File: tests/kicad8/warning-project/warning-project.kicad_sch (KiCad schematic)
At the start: 0 parts

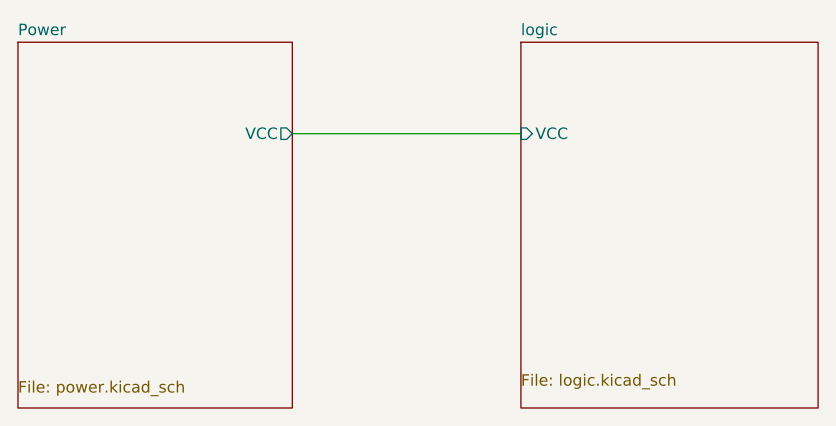
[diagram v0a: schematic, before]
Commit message: [PCBNew][DRC] Implemented CLI version
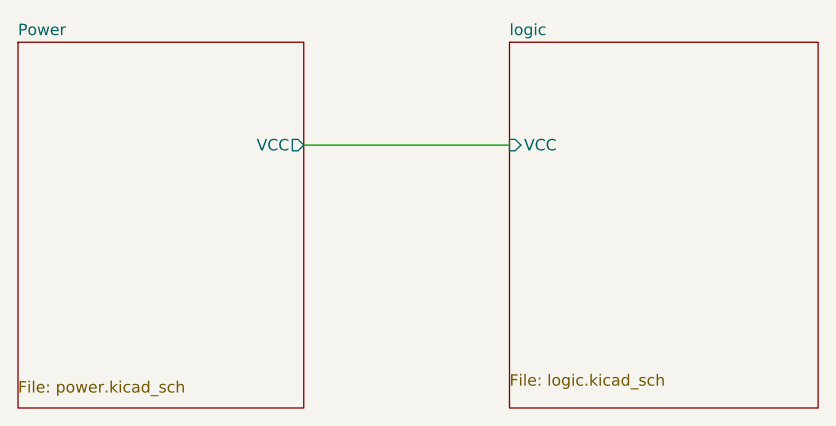
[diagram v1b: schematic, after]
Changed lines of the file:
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@@
-(kicad_sch (version 20230409) (generator eeschema)
-  (paper "A4")
-  (wire (pts (xy 111.76 63.5) (xy 137.16 63.5))
-    (stroke (width 0) (type default))
-  )
-  (sheet (at 81.28 53.34) (size 30.48 40.64)
-    (stroke (width 0) (type solid))
-    (fill (color 0 0 0 0.0000))
-    (property "Sheetname" "Power" (at 81.28 52.7045 0)
-      (effects (font (size 1.27 1.27)) (justify left bottom))
-    )
-    (property "Sheetfile" "power.kicad_sch" (at 81.28 90.9325 0)
-      (effects (font (size 1.27 1.27)) (justify left top))
-    )
-    (pin "VCC" output (at 111.76 63.5 0)
-      (effects (font (size 1.27 1.27)) (justify right))
-    )
-    (instances
-      (project "warning-project"
-        (path "/87c78429-be2b-40ed-8d3b-56cb9666a56f" (page "2"))
-      )
-    )
-  )
-  (sheet (at 137.16 53.34) (size 33.02 40.64)
-    (stroke (width 0) (type solid))
-    (fill (color 0 0 0 0.0000))
-    (property "Sheetname" "logic" (at 137.16 52.7045 0)
-      (effects (font (size 1.27 1.27)) (justify left bottom))
-    )
-    (property "Sheetfile" "logic.kicad_sch" (at 137.16 90.1705 0)
-      (effects (font (size 1.27 1.27)) (justify left top))
-    )
-    (pin "VCC" input (at 137.16 63.5 180)
-      (effects (font (size 1.27 1.27)) (justify left))
-    )
-    (instances
-      (project "warning-project"
-        (path "/87c78429-be2b-40ed-8d3b-56cb9666a56f" (page "3"))
-      )
-    )
-  )
-  (sheet_instances
-    (path "/" (page "1"))
-  )
+(kicad_sch
+	(version 20231120)
+	(generator "eeschema")
+	(generator_version "8.0")
+	(paper "A4")
+	(wire
+		(pts
+			(xy 113.03 64.77) (xy 135.89 64.77)
+		)
+		(stroke
+			(width 0)
+			(type default)
+		)
+	)
+	(sheet
+		(at 81.28 53.34)
+		(size 31.75 40.64)
+		(stroke
+			(width 0)
+			(type solid)
+		)
+		(fill
+			(color 0 0 0 0.0000)
+		)
+		(property "Sheetname" "Power"
+			(at 81.28 52.7045 0)
+			(effects
+				(font
+					(size 1.27 1.27)
+				)
+				(justify left bottom)
+			)
+		)
+		(property "Sheetfile" "power.kicad_sch"
+			(at 81.28 90.9325 0)
+			(effects
+				(font
+					(size 1.27 1.27)
+				)
+				(justify left top)
+			)
+		)
+		(pin "VCC" output
+			(at 113.03 64.77 0)
+			(effects
+				(font
+					(size 1.27 1.27)
+				)
+				(justify right)
+			)
+		)
+		(instances
+			(project "fail-project"
+				(path "/87c78429-be2b-40ed-8d3b-56cb9666a56f"
+					(page "2")
+				)
+			)
+		)
+	)
+	(sheet
+		(at 135.89 53.34)
+		(size 34.29 40.64)
+		(stroke
+			(width 0)
+			(type solid)
+		)
+		(fill
+			(color 0 0 0 0.0000)
+		)
+		(property "Sheetname" "logic"
+			(at 135.89 52.7045 0)
+			(effects
+				(font
+					(size 1.27 1.27)
+				)
+				(justify left bottom)
+			)
+		)
+		(property "Sheetfile" "logic.kicad_sch"
+			(at 135.89 90.1705 0)
+			(effects
+				(font
+					(size 1.27 1.27)
+				)
+				(justify left top)
+			)
+		)
+		(pin "VCC" input
+			(at 135.89 64.77 180)
+			(effects
+				(font
+					(size 1.27 1.27)
+				)
+				(justify left)
+			)
+		)
+		(instances
+			(project "fail-project"
+				(path "/87c78429-be2b-40ed-8d3b-56cb9666a56f"
+					(page "3")
+				)
+			)
+		)
+	)
+	(sheet_instances
+		(path "/"
+			(page "1")
+		)
+	)
 )
